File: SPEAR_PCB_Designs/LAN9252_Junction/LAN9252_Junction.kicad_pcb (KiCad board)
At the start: 2 copper layers, 68 parts, among them J1 SM04B-GHS-TB, J3 SM04B-GHS-TB, SW2 SW_MEC_5E, T1 H1102NLT, T2 H1102NLT, U1 LAN9252_ML, U2 24FC512, Y1 25MHz

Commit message: Almost finished board
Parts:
- added C28: 1000 pF, Capacitor_SMD:C_0402_1005Metric, F.Cu at (111.5, 108.8)
- added C29: 1000 pF, Capacitor_SMD:C_0402_1005Metric, F.Cu at (70.3, 38.9)
- added C30: 0.1 uF, Capacitor_SMD:C_0402_1005Metric, F.Cu at (70.1, 60.9)
- added C31: 18pF, Capacitor_SMD:C_0402_1005Metric, F.Cu at (72.0, 69.7)
- added C32: 0.1uF, Capacitor_SMD:C_0402_1005Metric, F.Cu at (107.7, 60.7)
- added C33: 0.1uF, Capacitor_SMD:C_0402_1005Metric, F.Cu at (83.5, 60.8)
- added C34: 18pF, Capacitor_SMD:C_0402_1005Metric, F.Cu at (74.0, 86.5)
- added C35: 0.1uF, Capacitor_SMD:C_0402_1005Metric, F.Cu at (85.2, 60.4)
- added C36: 0.1uF, Capacitor_SMD:C_0402_1005Metric, F.Cu at (87.1, 58.5)
- added C37: 1uF, Capacitor_SMD:C_0402_1005Metric, F.Cu at (100.2, 70.8)
- added C38: 0.1uF, Capacitor_SMD:C_0402_1005Metric, F.Cu at (87.2, 60.4)
- added C39: 0.1uF, Capacitor_SMD:C_0402_1005Metric, F.Cu at (83.9, 64.4)
- added C40: 470 pF, Capacitor_SMD:C_0402_1005Metric, F.Cu at (82.7, 64.5)
- added C41: 0.1uF, Capacitor_SMD:C_0402_1005Metric, F.Cu at (85.9, 67.6)
- added C42: 0.1uF, Capacitor_SMD:C_0402_1005Metric, F.Cu at (99.9, 67.3)
- added C43: 0.1uF, Capacitor_SMD:C_0402_1005Metric, F.Cu at (100.6, 68.9)
- added C44: 0.1uF, Capacitor_SMD:C_0402_1005Metric, F.Cu at (99.7, 79.0)
- added C45: 0.1uF, Capacitor_SMD:C_0402_1005Metric, F.Cu at (85.8, 69.0)
- added C46: 0.1uF, Capacitor_SMD:C_0402_1005Metric, F.Cu at (86.2, 64.2)
- added C47: 0.1uF, Capacitor_SMD:C_0402_1005Metric, F.Cu at (84.6, 77.1)
- added C48: 10p, Capacitor_SMD:C_0402_1005Metric, F.Cu at (108.2, 55.6)
- added C49: 10p, Capacitor_SMD:C_0402_1005Metric, F.Cu at (89.5, 55.6)
- added C50: 10p, Capacitor_SMD:C_0402_1005Metric, F.Cu at (110.5, 55.6)
- added C51: 10p, Capacitor_SMD:C_0402_1005Metric, F.Cu at (87.3, 55.5)
- added C52: 10p, Capacitor_SMD:C_0402_1005Metric, F.Cu at (101.8, 55.6)
- added C53: 10p, Capacitor_SMD:C_0402_1005Metric, F.Cu at (96.0, 55.5)
- added C54: 10p, Capacitor_SMD:C_0402_1005Metric, F.Cu at (104.1, 55.6)
- added C55: 10p, Capacitor_SMD:C_0402_1005Metric, F.Cu at (93.4, 55.5)
- added C56: 22n, Capacitor_SMD:C_0402_1005Metric, F.Cu at (102.2, 60.8)
- added C57: 22n, Capacitor_SMD:C_0402_1005Metric, F.Cu at (80.7, 59.1)
- added C58: 1000 pF, Capacitor_SMD:C_0402_1005Metric, F.Cu at (85.0, 38.8)
- added C59: 1000 pF, Capacitor_SMD:C_0402_1005Metric, F.Cu at (99.7, 38.8)
- added C60: 0.1 uF, Capacitor_SMD:C_0402_1005Metric, F.Cu at (99.4, 68.9)
- added C61: 10uF, Capacitor_SMD:C_0805_2012Metric, F.Cu at (121.6, 91.2)
- added C62: 10uF, Capacitor_SMD:C_0805_2012Metric, F.Cu at (121.6, 94.2)
- added C63: 150nF, SPEAR_MOTORCONTRLLER:CAP_CC1206_YAG, F.Cu at (128.8, 81.6)
- added C64: 22uF, SPEAR_MOTORCONTRLLER:CAP_C3225X7R1C226M250AC, F.Cu at (128.8, 73.8)
- added C65: 22uF, SPEAR_MOTORCONTRLLER:CAP_C3225X7R1C226M250AC, F.Cu at (128.8, 77.8)
- added C66: 0.1uF, Capacitor_SMD:C_0201_0603Metric, F.Cu at (128.2, 122.7)
- added C67: 0.1uF, Capacitor_SMD:C_0201_0603Metric, F.Cu at (138.3, 112.3)
- added D4: LED, LED_SMD:LED_0603_1608Metric, F.Cu at (97.3, 39.0)
- added D5: LED, LED_SMD:LED_0603_1608Metric, F.Cu at (111.9, 39.0)
- added D6: LED, LED_SMD:LED_0603_1608Metric, F.Cu at (113.1, 65.2)
- added F1: 10A, SPEAR_MOTORCONTRLLER:3557-15_KEY, F.Cu at (132.6, 45.1)
- added F2: 15A, SPEAR_MOTORCONTRLLER:3557-15_KEY, F.Cu at (132.6, 53.5)
- added F3: 2A, SPEAR_MOTORCONTRLLER:FUSE_36912000440, F.Cu at (155.1, 45.4)
- added FB5: BLM18EG221SN1D, SPEAR_FOOTPRINTS:Ferrite_bead, F.Cu at (105.3, 61.6)
- added FB6: FerriteBead, SPEAR_FOOTPRINTS:Ferrite_bead, F.Cu at (81.3, 61.1)
- added FB7: BLM18EG221SN1D, SPEAR_FOOTPRINTS:Ferrite_bead, F.Cu at (84.2, 58.2)
- added FB8: BLM18EG221SN1D, SPEAR_FOOTPRINTS:Ferrite_bead, F.Cu at (82.6, 66.2)
- added J2: SM04B-GHS-TB, Connector_JST:JST_GH_SM04B-GHS-TB_1x04-1MP_P1.25mm_Horizontal, F.Cu at (77.0, 39.4)
- added J4: SM04B-GHS-TB, Connector_JST:JST_GH_SM04B-GHS-TB_1x04-1MP_P1.25mm_Horizontal, F.Cu at (106.2, 39.4)
- added J5: Conn_01x02_Pin, SPEAR_MOTORCONTRLLER:AMASS_XT30PW-M_1x02_P2.50mm_Horizontal_1, F.Cu at (138.0, 39.8)
- added J6: Conn_01x02_Pin, SPEAR_MOTORCONTRLLER:AMASS_XT30PW-M_1x02_P2.50mm_Horizontal_1, F.Cu at (153.4, 39.8)
- added R22: 1k, Resistor_SMD:R_0402_1005Metric, F.Cu at (83.2, 41.2)
- added R23: 4.7kR, Resistor_SMD:R_0402_1005Metric, F.Cu at (70.0, 69.7)
- added R24: 10kR, Resistor_SMD:R_0402_1005Metric, F.Cu at (97.8, 96.2)
- added R30: 0R, Resistor_SMD:R_0402_1005Metric, F.Cu at (75.2, 69.7)
- added R31: 12.1k, Resistor_SMD:R_0402_1005Metric, F.Cu at (91.9, 59.1)
- added R32: 141 R, Resistor_SMD:R_0402_1005Metric, F.Cu at (81.6, 68.2)
- added R33: 141 R, Resistor_SMD:R_0402_1005Metric, F.Cu at (167.0, 64.5)
- added R34: 49.9R 1%, Resistor_SMD:R_0402_1005Metric, F.Cu at (108.2, 56.8)
- added R35: 49.9R 1%, Resistor_SMD:R_0402_1005Metric, F.Cu at (89.5, 56.7)
- added R36: 49.9R 1%, Resistor_SMD:R_0402_1005Metric, F.Cu at (110.6, 56.8)
- added R37: 49.9R 1%, Resistor_SMD:R_0402_1005Metric, F.Cu at (87.2, 56.6)
- added R38: 49.9R 1%, Resistor_SMD:R_0402_1005Metric, F.Cu at (101.8, 56.8)
- added R39: 49.9R 1%, Resistor_SMD:R_0402_1005Metric, F.Cu at (96.0, 56.7)
- added R40: 49.9R 1%, Resistor_SMD:R_0402_1005Metric, F.Cu at (104.1, 56.8)
- added R41: 49.9R 1%, Resistor_SMD:R_0402_1005Metric, F.Cu at (93.4, 56.7)
- added R42: 0R, Resistor_SMD:R_0402_1005Metric, F.Cu at (105.6, 60.2)
- added R43: 0R, Resistor_SMD:R_0402_1005Metric, F.Cu at (81.9, 59.1)
- added R44: 1k, Resistor_SMD:R_0402_1005Metric, F.Cu at (97.8, 41.2)
- added R45: 75R 1%, Resistor_SMD:R_0402_1005Metric, F.Cu at (85.0, 40.9)
- added R46: 75R 1%, Resistor_SMD:R_0402_1005Metric, F.Cu at (86.2, 40.9)
- added R47: 75R 1%, Resistor_SMD:R_0402_1005Metric, F.Cu at (99.7, 40.9)
- added R48: 75R 1%, Resistor_SMD:R_0402_1005Metric, F.Cu at (100.8, 40.9)
- added R49: 1k, Resistor_SMD:R_0402_1005Metric, F.Cu at (112.4, 41.2)
- added R50: 4.7kR, Resistor_SMD:R_0402_1005Metric, F.Cu at (110.3, 62.1)
- added R51: 10kR, Resistor_SMD:R_0402_1005Metric, F.Cu at (113.9, 62.5)
- added R52: 10kR, Resistor_SMD:R_0402_1005Metric, F.Cu at (112.4, 42.9)
- added R53: 10kR, Resistor_SMD:R_0402_1005Metric, F.Cu at (97.7, 42.9)
- added R54: 270R, Resistor_SMD:R_0402_1005Metric, F.Cu at (112.9, 62.5)
- added R55: 2kR, Resistor_SMD:R_0402_1005Metric, F.Cu at (105.1, 69.8)
- added R56: 2kR, Resistor_SMD:R_0402_1005Metric, F.Cu at (105.1, 68.6)
- added R57: 10k, Resistor_SMD:R_0402_1005Metric, F.Cu at (124.7, 122.7)
- added R58: 10k, Resistor_SMD:R_0402_1005Metric, F.Cu at (134.9, 112.3)
- added SW1: SW_MEC_5E, Button_Switch_THT:SW_PUSH_6mm, F.Cu at (121.3, 125.0)
- added T3: H1102NLT, SPEAR_FOOTPRINTS:XFMR_H1102NLT, F.Cu at (91.6, 49.0)
- added T4: H1102NLT, SPEAR_FOOTPRINTS:XFMR_H1102NLT, F.Cu at (106.2, 49.0)
- added U3: LAN9252_ML, SPEAR_FOOTPRINTS:LAN9252_QFN UPDATED, F.Cu at (92.1, 66.3)
- added U4: 24FC512, Package_SO:SOIC-8_3.9x4.9mm_P1.27mm, F.Cu at (108.8, 66.4)
- added U5: AP63203WU, SPEAR_MOTORCONTRLLER:AP63203WU-7_DIO-L, F.Cu at (124.7, 62.8)
- added Y2: 25MHz, SPEAR_FOOTPRINTS:Y_Wurth_WE-XTAL_Quartz-HC49-4HSMX, F.Cu at (73.6, 78.2)
- C1: value 1uF -> 18pF; footprint Capacitor_SMD:C_0201_0603Metric -> Capacitor_SMD:C_0402_1005Metric
- C10: value 0.1uF -> 470 pF; footprint Capacitor_SMD:C_0201_0603Metric -> Capacitor_SMD:C_0402_1005Metric
- C11, C12, C13, C14, C15, C16, C17, C2, C5, C8, C9: footprint Capacitor_SMD:C_0201_0603Metric -> Capacitor_SMD:C_0402_1005Metric
- C18, C19, C20, C21, C22: value 0.1uF -> 10p; footprint Capacitor_SMD:C_0201_0603Metric -> Capacitor_SMD:C_0402_1005Metric
- C23, C24: value C -> 10p; footprint Capacitor_SMD:C_0201_0603Metric -> Capacitor_SMD:C_0402_1005Metric
- C25: value 1000 uF -> 10p; footprint Capacitor_SMD:C_0201_0603Metric -> Capacitor_SMD:C_0402_1005Metric
- C26: value 1000 uF -> 22n; footprint Capacitor_SMD:C_0201_0603Metric -> Capacitor_SMD:C_0402_1005Metric
- C27: value 0.1 uF -> 22n; footprint Capacitor_SMD:C_0201_0603Metric -> Capacitor_SMD:C_0402_1005Metric
- C3: value 1uF -> 0.1uF; footprint Capacitor_SMD:C_0201_0603Metric -> Capacitor_SMD:C_0402_1005Metric
- C4: value 0.1uF -> 18pF; footprint Capacitor_SMD:C_0201_0603Metric -> Capacitor_SMD:C_0402_1005Metric
- C6: value 18pF -> 0.1uF; footprint Capacitor_SMD:C_0201_0603Metric -> Capacitor_SMD:C_0402_1005Metric
- C7: value 18pF -> 1uF; footprint Capacitor_SMD:C_0201_0603Metric -> Capacitor_SMD:C_0402_1005Metric
- D1, D2, D3: footprint LED_SMD:LED_0201_0603Metric -> LED_SMD:LED_0603_1608Metric
- FB1, FB2, FB3, FB4: footprint Footprints SPEAR:Ferrite_bead -> SPEAR_FOOTPRINTS:Ferrite_bead
- R1: value 12.1k -> 4K7; footprint Resistor_SMD:R_0603_1608Metric -> Resistor_SMD:R_0402_1005Metric
- R10, R11, R12, R7, R8, R9: value 49.9 R -> 49.9R 1%; footprint Resistor_SMD:R_0603_1608Metric -> Resistor_SMD:R_0402_1005Metric
- R13, R14: value 2kR -> 49.9R 1%; footprint Resistor_SMD:R_0603_1608Metric -> Resistor_SMD:R_0402_1005Metric
- R15: value 4.7kR -> 0R; footprint Resistor_SMD:R_0603_1608Metric -> Resistor_SMD:R_0402_1005Metric
- R16: value 270R -> 0R; footprint Resistor_SMD:R_0603_1608Metric -> Resistor_SMD:R_0402_1005Metric
- R17: value 10kR -> 1k; footprint Resistor_SMD:R_0603_1608Metric -> Resistor_SMD:R_0402_1005Metric
- R18, R19: value 10kR -> 75R 1%; footprint Resistor_SMD:R_0603_1608Metric -> Resistor_SMD:R_0402_1005Metric
- R2: value 10k -> 4K7; footprint Resistor_SMD:R_0603_1608Metric -> Resistor_SMD:R_0402_1005Metric
- R20, R21: value 1k -> 75R 1%; footprint Resistor_SMD:R_0603_1608Metric -> Resistor_SMD:R_0402_1005Metric
- R25: value 0R -> 10kR; footprint Resistor_SMD:R_0603_1608Metric -> Resistor_SMD:R_0402_1005Metric
- R26: value 75 -> 10kR; footprint Resistor_SMD:R_0603_1608Metric -> Resistor_SMD:R_0402_1005Metric
- R27: value 75 -> 270R; footprint Resistor_SMD:R_0603_1608Metric -> Resistor_SMD:R_0402_1005Metric
- R28, R29: value 75 -> 2kR; footprint Resistor_SMD:R_0603_1608Metric -> Resistor_SMD:R_0402_1005Metric
- R3: value 49.9 R -> 0R; footprint Resistor_SMD:R_0603_1608Metric -> Resistor_SMD:R_0402_1005Metric
- R4: value 49.9 R -> 12.1k; footprint Resistor_SMD:R_0603_1608Metric -> Resistor_SMD:R_0402_1005Metric
- R5, R6: value 49.9 R -> 141 R; footprint Resistor_SMD:R_0603_1608Metric -> Resistor_SMD:R_0402_1005Metric
- T1, T2: footprint Transformer_SMD:Transformer_Pulse_H1100NL -> SPEAR_FOOTPRINTS:XFMR_H1102NLT
- U1: footprint Footprints SPEAR:QFP50P1200X1200X120-65N -> SPEAR_FOOTPRINTS:LAN9252_QFN UPDATED
- Y1: footprint Crystal:Crystal_HC50_Vertical -> SPEAR_FOOTPRINTS:Y_Wurth_WE-XTAL_Quartz-HC49-4HSMX
- moved D2 65.7 mm to (82.7, 39.0), turned to -90 degrees
- moved T2 65.1 mm to (76.9, 49.0), turned to 90 degrees
- moved C26 61.5 mm to (70.3, 57.7), turned to 180 degrees
- moved R21 57.9 mm to (71.5, 41.0), turned to 90 degrees
- moved SW2 57.3 mm to (131.4, 115.2)
- moved R20 57.1 mm to (70.3, 41.0), turned to 90 degrees
- moved C24 56.7 mm to (75.1, 55.2)
- moved J3 54.7 mm to (91.5, 39.5), turned to 180 degrees
- moved C22 52.0 mm to (72.5, 55.2), turned to 180 degrees
- moved FB1 51.1 mm to (75.0, 60.4), turned to 90 degrees
- moved R29 50.4 mm to (73.5, 60.4), turned to -90 degrees
- moved R28 49.9 mm to (72.2, 60.4), turned to -90 degrees
- moved U2 48.8 mm to (71.6, 65.2), turned to 90 degrees
- moved R15 47.6 mm to (70.3, 58.9), turned to 180 degrees
- moved C18 44.9 mm to (78.7, 55.1), turned to 180 degrees
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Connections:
- net /D0/SIO0 renamed /LAN9252 System 1/D0/SIO0
- net /D1/SIO1 renamed /LAN9252 System 1/D1/SIO1
- net /D2/SIO2 renamed /LAN9252 System 1/D2/SIO2
- net /D3/SIO3 renamed /LAN9252 System 1/D3/SIO3
- net /D5/OUTVALID/~{SCS} renamed /LAN9252 System 1/D5/OUTVALID/~{SCS}
- net /D7/GPI1/GPO1 renamed /LAN9252 System 1/MII_MDC
- net /D9/LATCH_IN/SCK renamed /LAN9252 System 1/D9/LATCH_IN/SCK
- net /IRQ renamed /LAN9252 System 1/IRQ
- net /SYNC0/LATCH0 renamed /LAN9252 System 1/SYNC0/LATCH0
- net /SYNC1/LATCH1 renamed /LAN9252 System 1/SYNC1/LATCH1
- C1 pad 1: /VDD33TXRX1 -> GND
- C10 pad 1: /VDD12TX1 -> /LAN9252 System 1/VDDCR
- C10 pad 2: GNDREF -> GND
- C11 pad 1: /VDD12TX1 -> +3.3V
- C11 pad 2: GNDREF -> GND
- C12 pad 1: +3.3V -> /LAN9252 System 1/VDDCR
- C12 pad 2: GNDREF -> GND
- C13 pad 2: GNDREF -> GND
- C14 pad 2: GNDREF -> GND
- C15 pad 2: GNDREF -> GND
- C16 pad 2: GNDREF -> GND
- C17 pad 2: GNDREF -> GND
- C18 pad 1: /VDDCR -> /LAN9252 System 1/TXA_P
- C18 pad 2: GNDREF -> GND
- C19 pad 1: /VDDCR -> /LAN9252 System 1/TXB_P
- C19 pad 2: GNDREF -> GND
- C2 pad 1: /VDD33TXRX1 -> /LAN9252 System 1/VDD33TXRX1
- C2 pad 2: Net-(C1-Pad2) -> GND
- C20 pad 1: /VDDCR -> /LAN9252 System 1/TXA_N
- C20 pad 2: GNDREF -> GND
- C21 pad 1: /VDDCR -> /LAN9252 System 1/TXB_N
- C21 pad 2: GNDREF -> GND
- C22 pad 1: /TP3 -> /LAN9252 System 1/RXA_P
- C22 pad 2: GNDREF -> GND
- C23 pad 1: Net-(C23-Pad1) -> /LAN9252 System 1/RXB_P
- C23 pad 2: GNDREF -> GND
- C24 pad 1: Net-(C24-Pad1) -> /LAN9252 System 1/RXA_N
- C24 pad 2: GNDREF -> GND
- C25 pad 1: Net-(C25-Pad1) -> /LAN9252 System 1/RXB_N
- C25 pad 2: GNDREF -> GND
- C26 pad 2: GNDREF -> GND
- C27 pad 1: +3.3V -> Net-(C27-Pad1)
- C27 pad 2: GNDREF -> GND
- C3 pad 1: /VDD33TXRX2 -> /LAN9252 System 1/VDD33TXRX2
- C3 pad 2: Net-(C3-Pad2) -> GND
- C4 pad 1: /VDD33TXRX2 -> GND
- C4 pad 2: Net-(C3-Pad2) -> Net-(U1-OSCO)
- C5 pad 1: +3.3V -> Net-(U1-VDD33BIAS)
- C6 pad 1: GNDREF -> /LAN9252 System 1/VDD12TX1
- C6 pad 2: Net-(C6-Pad2) -> GND
- C7 pad 1: GNDREF -> /LAN9252 System 1/VDDCR
- C7 pad 2: Net-(U1-OSCO) -> GND
- C8 pad 1: /VDD12TX1 -> /LAN9252 System 1/VDD12TX1
- C8 pad 2: GNDREF -> GND
- C9 pad 1: /VDD12TX1 -> /LAN9252 System 1/VDDCR
- C9 pad 2: GNDREF -> GND
- D1 pad 1: Net-(D1-K) -> GND
- D1 pad 2: +3.3V -> Net-(D1-A)
- D2 pad 1: Net-(D2-K) -> GND
- D2 pad 2: GND -> Net-(D2-A)
- D3 pad 2: GND -> +3.3V
- FB1 pad 2: /VDD33TXRX1 -> /LAN9252 System 1/VDD33TXRX1
- FB2 pad 2: /VDD33TXRX2 -> /LAN9252 System 1/VDD33TXRX2
- FB4 pad 1: /VDD12TX1 -> /LAN9252 System 1/VDD12TX1
- FB4 pad 2: /VDDCR -> /LAN9252 System 1/VDDCR
- J1 pad 1: Net-(J1-Pin_1) -> /LAN9252 System 1/LAN9252 Ports/TXB+
- J1 pad 2: Net-(J1-Pin_2) -> /LAN9252 System 1/LAN9252 Ports/TXB-
- J1 pad 3: Net-(J1-Pin_3) -> /LAN9252 System 1/LAN9252 Ports/RXB+
- J1 pad 4: Net-(J1-Pin_4) -> /LAN9252 System 1/LAN9252 Ports/RXB-
- J3 pad 1: Net-(J3-Pin_1) -> /LAN9252 System 2/LAN9252 Ports/TXB+
- J3 pad 2: Net-(J3-Pin_2) -> /LAN9252 System 2/LAN9252 Ports/TXB-
- J3 pad 3: Net-(J3-Pin_3) -> /LAN9252 System 2/LAN9252 Ports/RXB+
- J3 pad 4: Net-(J3-Pin_4) -> /LAN9252 System 2/LAN9252 Ports/RXB-
- R1 pad 1: GNDREF -> /LAN9252 System 1/MII_MDIO
- R1 pad 2: Net-(U1-RBIAS) -> +3.3V
- R10 pad 1: /VDD33TXRX2 -> /LAN9252 System 1/VDD33TXRX2
- R10 pad 2: /RXB_P -> /LAN9252 System 1/TXB_N
- R11 pad 1: /VDD33TXRX2 -> /LAN9252 System 1/VDD33TXRX1
- R11 pad 2: /RXB_N -> /LAN9252 System 1/RXA_P
- R12 pad 1: /VDD33TXRX2 -> /LAN9252 System 1/VDD33TXRX2
- R12 pad 2: Net-(C24-Pad1) -> /LAN9252 System 1/RXB_P
- R13 pad 1: +3.3V -> /LAN9252 System 1/VDD33TXRX1
- R13 pad 2: /I2C_SCL -> /LAN9252 System 1/RXA_N
- R14 pad 1: +3.3V -> /LAN9252 System 1/VDD33TXRX2
- R14 pad 2: /I2C_SDL -> /LAN9252 System 1/RXB_N
- R15 pad 1: GNDREF -> /LAN9252 System 1/VDD33TXRX1
- R15 pad 2: Net-(U2-A0) -> Net-(C26-Pad1)
- R16 pad 1: /GPIO2 -> /LAN9252 System 1/VDD33TXRX2
- R16 pad 2: Net-(D1-K) -> Net-(C27-Pad1)
- R17 pad 1: /GPIO2 -> /LAN9252 System 1/GPIO1
- R17 pad 2: +3.3V -> Net-(D1-A)
- R18 pad 1: GNDREF -> Net-(R18-Pad1)
- R18 pad 2: /GPIO0 -> Net-(C28-Pad1)
- R19 pad 1: GNDREF -> Net-(R19-Pad1)
- R19 pad 2: /GPIO1 -> Net-(C28-Pad1)
- R2 pad 1: +3.3V -> /LAN9252 System 2/MII_MDIO
- R2 pad 2: /TP3 -> +3.3V
- R20 pad 1: /GPIO1 -> Net-(R20-Pad1)
- R20 pad 2: Net-(D2-K) -> Net-(C29-Pad1)
- R21 pad 1: /GPIO0 -> Net-(R21-Pad1)
- R21 pad 2: Net-(D3-K) -> Net-(C29-Pad1)
- R25 pad 1: Net-(C6-Pad2) -> GND
- R25 pad 2: Net-(U1-OSCI) -> /LAN9252 System 1/GPIO0
- R26 pad 1: Net-(R26-Pad1) -> +3.3V
- R26 pad 2: Net-(C26-Pad1) -> /LAN9252 System 1/GPIO1
- R27 pad 1: Net-(R27-Pad1) -> /LAN9252 System 1/GPIO2
- R27 pad 2: Net-(C26-Pad1) -> Net-(D3-K)
- R28 pad 1: Net-(R28-Pad1) -> +3.3V
- R28 pad 2: Net-(C25-Pad1) -> /LAN9252 System 1/I2C_SCL
- R29 pad 1: Net-(R29-Pad1) -> +3.3V
- R29 pad 2: Net-(C25-Pad1) -> /LAN9252 System 1/I2C_SDL
- R3 pad 1: /VDD33TXRX1 -> Net-(C1-Pad2)
- R3 pad 2: /TXA_P -> Net-(U1-OSCI)
- R4 pad 1: /VDD33TXRX1 -> GND
- R4 pad 2: /TXA_N -> Net-(U1-RBIAS)
- R5 pad 1: /VDD33TXRX1 -> /LAN9252 System 1/MII_TXD2
- R5 pad 2: /RXA_P -> GND
- R6 pad 1: /VDD33TXRX1 -> /LAN9252 System 1/MII_TXD3
- R6 pad 2: /RXA_N -> GND
- R7 pad 1: /VDD33TXRX1 -> /LAN9252 System 1/VDD33TXRX1
- R7 pad 2: Net-(C23-Pad1) -> /LAN9252 System 1/TXA_P
- R8 pad 1: /VDD33TXRX2 -> /LAN9252 System 1/VDD33TXRX2
- R8 pad 2: /TXB_P -> /LAN9252 System 1/TXB_P
- R9 pad 1: /VDD33TXRX2 -> /LAN9252 System 1/VDD33TXRX1
- R9 pad 2: /TXB_N -> /LAN9252 System 1/TXA_N
- SW2 pad 1: GNDREF -> GND
- SW2 pad 2: GNDREF -> GND
- SW2 pad 3: /TP3 -> /LAN9252 System 2/TP1
- SW2 pad 4: /TP3 -> /LAN9252 System 2/TP1
- T1 pad 1: /TXB_P -> /LAN9252 System 1/TXB_N
- T1 pad 10: Net-(R27-Pad1) -> Net-(R19-Pad1)
- T1 pad 11: Net-(J3-Pin_3) -> /LAN9252 System 1/LAN9252 Ports/TXB-
- T1 pad 14: Net-(J3-Pin_2) -> /LAN9252 System 1/LAN9252 Ports/RXB+
- T1 pad 15: Net-(R26-Pad1) -> Net-(R18-Pad1)
- T1 pad 16: Net-(J3-Pin_1) -> /LAN9252 System 1/LAN9252 Ports/RXB-
- T1 pad 2: Net-(C24-Pad1) -> Net-(C27-Pad1)
- T1 pad 3: /TXB_N -> /LAN9252 System 1/TXB_P
- T1 pad 6: /RXB_P -> /LAN9252 System 1/RXB_N
- T1 pad 7: Net-(C24-Pad1) -> Net-(C27-Pad1)
- T1 pad 8: /RXB_N -> /LAN9252 System 1/RXB_P
- T1 pad 9: Net-(J3-Pin_4) -> /LAN9252 System 1/LAN9252 Ports/TXB+
- T2 pad 1: /TXA_P -> /LAN9252 System 1/RXA_P
- T2 pad 10: Net-(R29-Pad1) -> Net-(R21-Pad1)
- T2 pad 11: Net-(J1-Pin_3) -> /LAN9252 System 1/LAN9252 Ports/TXA-
- T2 pad 14: Net-(J1-Pin_2) -> /LAN9252 System 1/LAN9252 Ports/RXA+
- T2 pad 15: Net-(R28-Pad1) -> Net-(R20-Pad1)
- T2 pad 16: Net-(J1-Pin_1) -> /LAN9252 System 1/LAN9252 Ports/RXA-
- T2 pad 2: Net-(C23-Pad1) -> Net-(C26-Pad1)
- T2 pad 3: /TXA_N -> /LAN9252 System 1/RXA_N
- T2 pad 6: /RXA_P -> /LAN9252 System 1/TXA_P
- T2 pad 7: Net-(C23-Pad1) -> Net-(C26-Pad1)
- T2 pad 8: /RXA_N -> /LAN9252 System 1/TXA_N
- T2 pad 9: Net-(J1-Pin_4) -> /LAN9252 System 1/LAN9252 Ports/TXA+
- U1 pad 10: unconnected-(U1-FXSDB/FXLOSB/~{FXSDENB}-Pad10) -> GND
- U1 pad 11: unconnected-(U1-~{RST}-Pad11) -> /LAN9252 System 1/RST#
- U1 pad 15: /D14/GPI8/GPO8/~{TX_SHIFT1} -> /LAN9252 System 1/MII_TXD3
- U1 pad 16: /D13/GPI7/GPO7/~{TX_SHIFT0} -> /LAN9252 System 1/MII_TXD2
- U1 pad 21: /D12/GPI6/GPO6 -> /LAN9252 System 1/MII_TXD1
- U1 pad 22: /D11/GPI5/GPO5 -> /LAN9252 System 1/MII_TXD0
- U1 pad 23: /D10/GPI4/GPO4 -> /LAN9252 System 1/MII_TXEN
- U1 pad 24: /VDDCR -> /LAN9252 System 1/VDDCR
- U1 pad 25: unconnected-(U1-A1/ALELO-Pad25) -> /LAN9252 System 1/MII_CLK25
- U1 pad 26: unconnected-(U1-A3/GPI11/GPO11-Pad26) -> /LAN9252 System 1/MII_RXDV
- U1 pad 27: unconnected-(U1-A4/GPI12/GPO12-Pad27) -> /LAN9252 System 1/MII_RXD0
- U1 pad 28: /CS -> /LAN9252 System 1/MII_RXD1
- U1 pad 29: unconnected-(U1-A2/ALEHI/GPI10/GPO10-Pad29) -> /LAN9252 System 1/MII_LINKPOL
- U1 pad 30: /WR/GPI14/GPO14 -> /LAN9252 System 1/MII_RXD2
- U1 pad 31: /RD/GPI15/GPO15 -> /LAN9252 System 1/MII_RXD3
- U1 pad 33: /A0/D15/GPI9/GPO9 -> GND
- U1 pad 36: /D6/GPI0/GPO0 -> /LAN9252 System 1/MII_RXCLK
- U1 pad 38: /VDDCR -> /LAN9252 System 1/VDDCR
- U1 pad 4: GNDREF -> GND
- U1 pad 40: /D8/GPI2/GPO2 -> /LAN9252 System 1/MII_MDIO
- U1 pad 41: GNDREF -> GND
- U1 pad 42: /I2C_SDL -> /LAN9252 System 1/I2C_SDL
- U1 pad 43: /I2C_SCL -> /LAN9252 System 1/I2C_SCL
- U1 pad 45: /GPIO2 -> /LAN9252 System 1/GPIO2
- U1 pad 46: /GPIO1 -> /LAN9252 System 1/GPIO1
- U1 pad 48: /GPIO0 -> /LAN9252 System 1/GPIO0
- U1 pad 49: /D4/GPI3/GPO3 -> /LAN9252 System 1/MII_LINK
- U1 pad 51: /VDD33TXRX1 -> /LAN9252 System 1/VDD33TXRX1
- U1 pad 52: /TXA_N -> /LAN9252 System 1/TXA_N
- U1 pad 53: /TXA_P -> /LAN9252 System 1/TXA_P
- U1 pad 54: /RXA_N -> /LAN9252 System 1/RXA_N
- U1 pad 55: /RXA_P -> /LAN9252 System 1/RXA_P
- U1 pad 56: /VDD12TX1 -> /LAN9252 System 1/VDD12TX1
- U1 pad 59: /VDD12TX1 -> /LAN9252 System 1/VDD12TX1
- U1 pad 6: /VDDCR -> /LAN9252 System 1/VDDCR
- U1 pad 60: /RXB_P -> /LAN9252 System 1/RXB_P
- U1 pad 61: /RXB_N -> /LAN9252 System 1/RXB_N
- U1 pad 62: /TXB_P -> /LAN9252 System 1/TXB_P
- U1 pad 63: /TXB_N -> /LAN9252 System 1/TXB_N
- U1 pad 64: /VDD33TXRX2 -> /LAN9252 System 1/VDD33TXRX2
- U1 pad 65: GNDREF -> GND
- U1 pad 8: GNDREF -> GND
- U1 pad 9: GNDREF -> GND
- U2 pad 4: GNDREF -> GND
- U2 pad 5: /I2C_SDL -> /LAN9252 System 1/I2C_SDL
- U2 pad 6: /I2C_SCL -> /LAN9252 System 1/I2C_SCL
- Y1 pad 2: Net-(C6-Pad2) -> Net-(C1-Pad2)
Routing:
- net GND: track 0.00 -> 83.2 mm, vias 0 -> 66
- net /LAN9252 System 1/GPIO0: track 0.00 -> 54.8 mm, vias 0 -> 2
- net +3.3V: track 0.00 -> 53.8 mm, vias 0 -> 27
- net /LAN9252 System 1/RXA_P: track 0.00 -> 48.5 mm
- net /LAN9252 System 1/VDD33TXRX1: track 0.00 -> 47.5 mm, vias 0 -> 3
- net /LAN9252 System 1/MII_LINK: track 0.00 -> 47.0 mm, vias 0 -> 2
- net /LAN9252 System 1/RXA_N: track 0.00 -> 46.0 mm
- net /LAN9252 System 1/TXA_P: track 0.00 -> 44.7 mm
- net /LAN9252 System 1/TXA_N: track 0.00 -> 43.8 mm
- net /LAN9252 System 1/GPIO1: track 0.00 -> 36.8 mm, vias 0 -> 3
- net /LAN9252 System 2/GPIO0: track 0.00 -> 36.8 mm, vias 0 -> 2
- net Net-(U3-OSCO): track 0.00 -> 35.9 mm, vias 0 -> 2
- net /LAN9252 System 2/VDDCR: track 0.00 -> 35.3 mm, vias 0 -> 4
- net /LAN9252 System 2/VDD33TXRX1: track 0.00 -> 32.7 mm, vias 0 -> 4
- net /LAN9252 System 1/VDD33TXRX2: track 0.00 -> 31.0 mm, vias 0 -> 4
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- added copper zone on In2.Cu, net +3.3V
- added copper zone on In1.Cu, net GND
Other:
- board outline added: 48 x 74.8 mm
- copper layers 2 -> 4

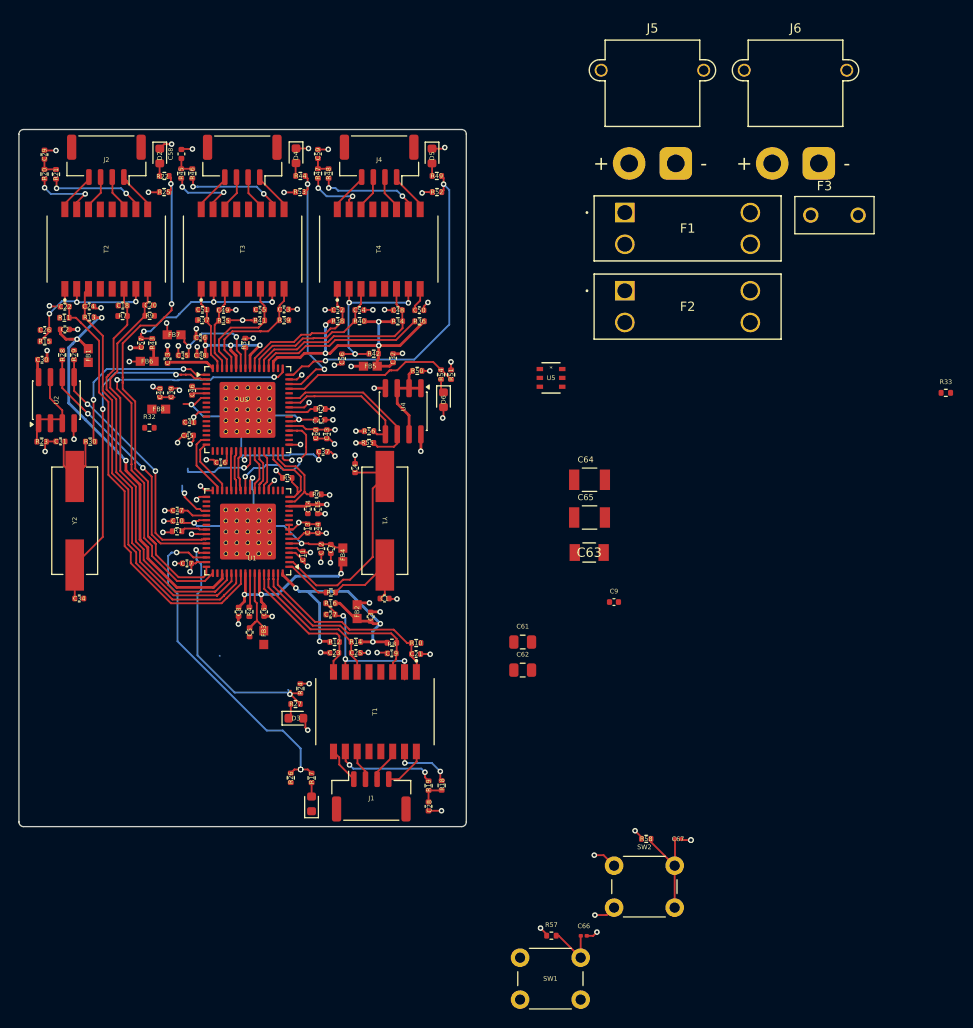
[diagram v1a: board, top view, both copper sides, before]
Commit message: Updated Junction board
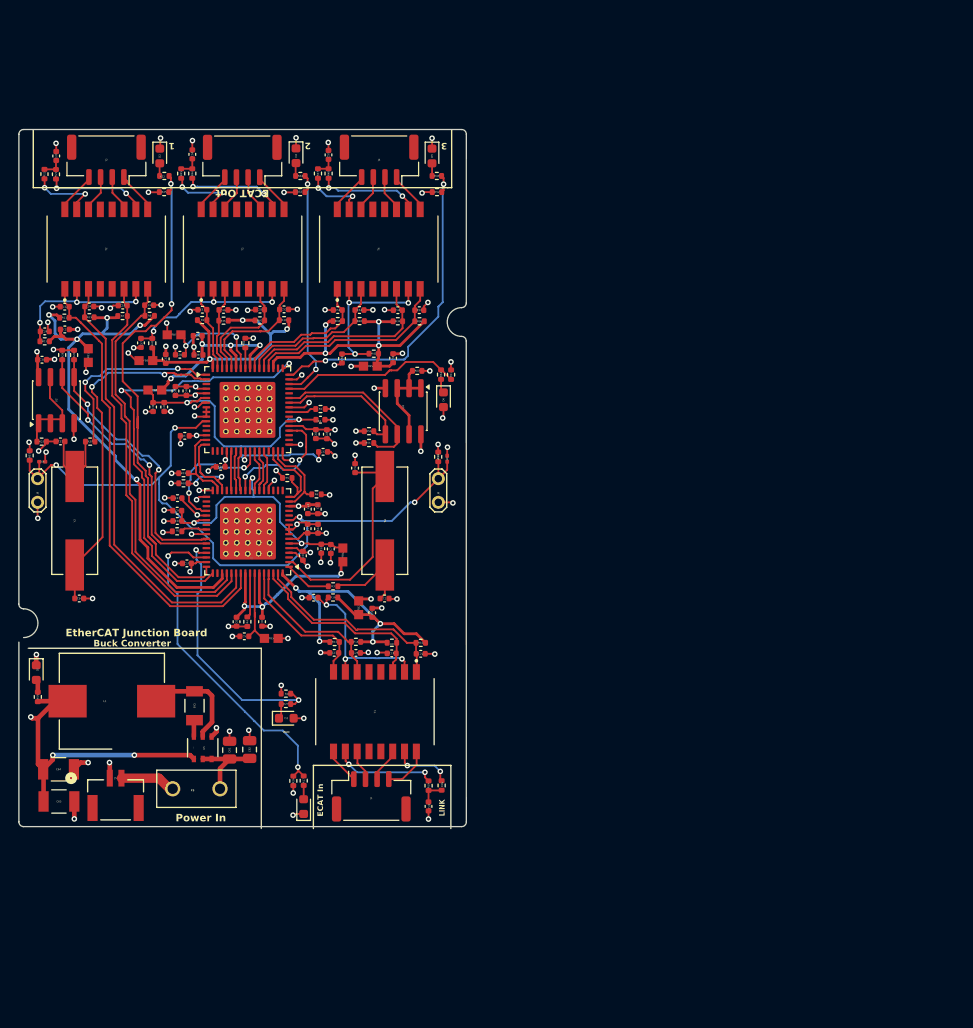
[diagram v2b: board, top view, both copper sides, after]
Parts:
- removed F1: 10A, SPEAR_MOTORCONTRLLER:3557-15_KEY
- removed F2: 15A, SPEAR_MOTORCONTRLLER:3557-15_KEY
- removed J6: Conn_01x02_Pin, SPEAR_MOTORCONTRLLER:AMASS_XT30PW-M_1x02_P2.50mm_Horizontal_1
- removed SW1, SW2: SW_MEC_5E, Button_Switch_THT:SW_PUSH_6mm
- added D7: LED, LED_SMD:LED_0603_1608Metric, F.Cu at (69.4, 94.5)
- added J8: Conn_01x02_Pin, TestPoint:TestPoint_2Pads_Pitch2.54mm_Drill0.8mm, F.Cu at (112.6, 73.7)
- added J9: Conn_01x02_Pin, TestPoint:TestPoint_2Pads_Pitch2.54mm_Drill0.8mm, F.Cu at (69.6, 73.7)
- added L1: 3.9uH, SPEAR_BUCK_CONVERTER:L_Wurth_WE-LHMI-1040_L1, F.Cu at (77.5, 97.5)
- added R59: 1k, Resistor_SMD:R_0402_1005Metric, F.Cu at (69.6, 97.1)
- J5: value Conn_01x02_Pin -> SM02B-GHS-TB; footprint SPEAR_MOTORCONTRLLER:AMASS_XT30PW-M_1x02_P2.50mm_Horizontal_1 -> SPEAR_POWERJUCTION:CONN_SM02B-GHS_JST
- moved F3 92.1 mm to (86.6, 106.9), turned to 180 degrees
- moved J5 91.0 mm to (77.9, 108.1)
- moved R33 82.2 mm to (85.2, 73.1), turned to 180 degrees
- moved C66 77.2 mm to (70.1, 71.8)
- moved R57 76.1 mm to (68.7, 71.2), turned to -90 degrees
- moved C64 64.9 mm to (71.8, 104.8)
- moved C65 64.6 mm to (71.9, 108.3)
- moved U5 54.5 mm to (87.3, 102.5), turned to 90 degrees
- moved C9 47.9 mm to (84.6, 77.1), turned to 180 degrees
- moved C67 47.7 mm to (113.5, 71.5), turned to 90 degrees
- moved R58 46.7 mm to (112.6, 71.3), turned to -90 degrees
- moved C63 45.4 mm to (86.4, 98.0), turned to -90 degrees
- moved C61 33.5 mm to (90.2, 102.8), turned to 90 degrees
- moved C62 30.5 mm to (92.3, 102.7), turned to 90 degrees
- moved R32 6.99 mm to (85.2, 74.2), turned to 180 degrees
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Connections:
- C66 pad 1: /LAN9252 System 1/TP1 -> /LAN9252 System 1/RST
- C67 pad 1: /LAN9252 System 2/TP1 -> /LAN9252 System 1/RST
- F3 pad 2: Net-(J6-Pin_2) -> Net-(F3-Pad2)
- J5 pad 2: Net-(J5-Pin_2) -> Net-(F3-Pad2)
- R57 pad 2: /LAN9252 System 1/TP1 -> /LAN9252 System 1/RST
- R58 pad 2: /LAN9252 System 2/TP1 -> /LAN9252 System 1/RST
- U1 pad 11: /LAN9252 System 1/RST# -> /LAN9252 System 1/RST
- U1 pad 49: /LAN9252 System 1/MII_LINK -> +3.3V
- U3 pad 11: /LAN9252 System 1/RST# -> /LAN9252 System 1/RST
- U3 pad 49: /LAN9252 System 1/MII_LINK -> +3.3V
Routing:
- net +3.3V: track 53.8 -> 145.7 mm, vias 27 -> 41
- net /LAN9252 System 1/RST: track 0.00 -> 77.8 mm, vias 0 -> 4
- net /LAN9252 System 1/MII_LINK: track 47.0 -> 0.00 mm, vias 2 -> 0
- net /LAN9252 System 2/VDD33TXRX2: track 9.59 -> 31.8 mm, vias 1 -> 3
- net GND: track 83.2 -> 104.8 mm, vias 66 -> 84
- net /LAN9252 System 1/VDD33TXRX1: track 47.5 -> 64.0 mm, vias 3 -> 5
- net /Buck Converter/SW: track 0.00 -> 11.6 mm
- net /LAN9252 System 2/TP1: track 11.3 -> 0.00 mm
- net /Buck Converter/BUCK_PWR: track 0.00 -> 9.92 mm
- net /LAN9252 System 2/VDD12TX1: track 13.5 -> 21.5 mm, vias 3 -> 4
- net Net-(F3-Pad2): track 0.00 -> 5.97 mm
- net /LAN9252 System 1/TP1: track 5.96 -> 0.00 mm
- net /LAN9252 System 1/VDD33TXRX2: track 31.0 -> 36.7 mm
- net /LAN9252 System 1/MII_RXD2: track 6.19 -> 11.7 mm, vias 0 -> 2
- net /LAN9252 System 2/VDDCR: track 35.3 -> 40.2 mm
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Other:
- outline, holes or cut-outs redrawn
- board text added: "1"
- board text added: "2"
- board text added: "3"
- board text added: "Buck Converter"
- board text added: "ECAT In"
- board text added: "ECAT Out"
- board text added: "EtherCAT Junction Board"
- board text added: "LINK"
- board text added: "Power In"
- board text added: "RUN"

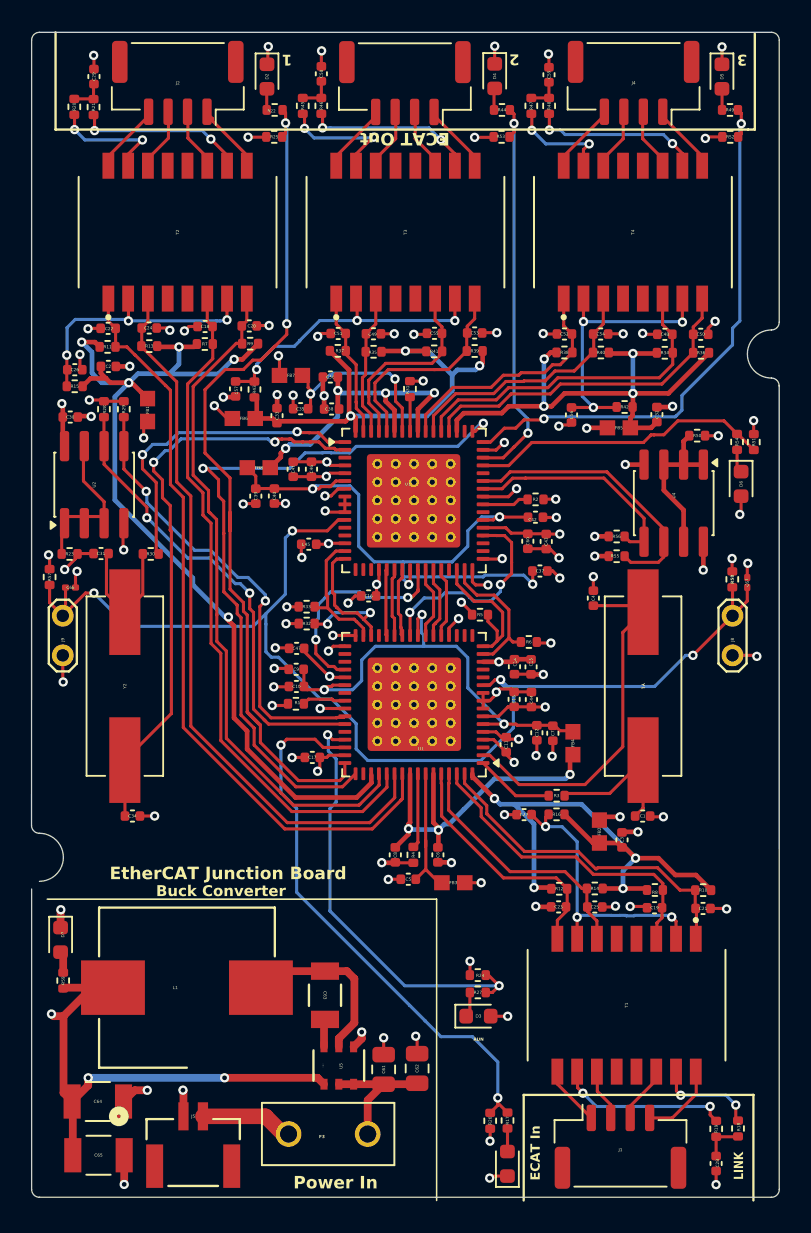
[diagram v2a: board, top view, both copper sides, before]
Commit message: Updated Junction Board
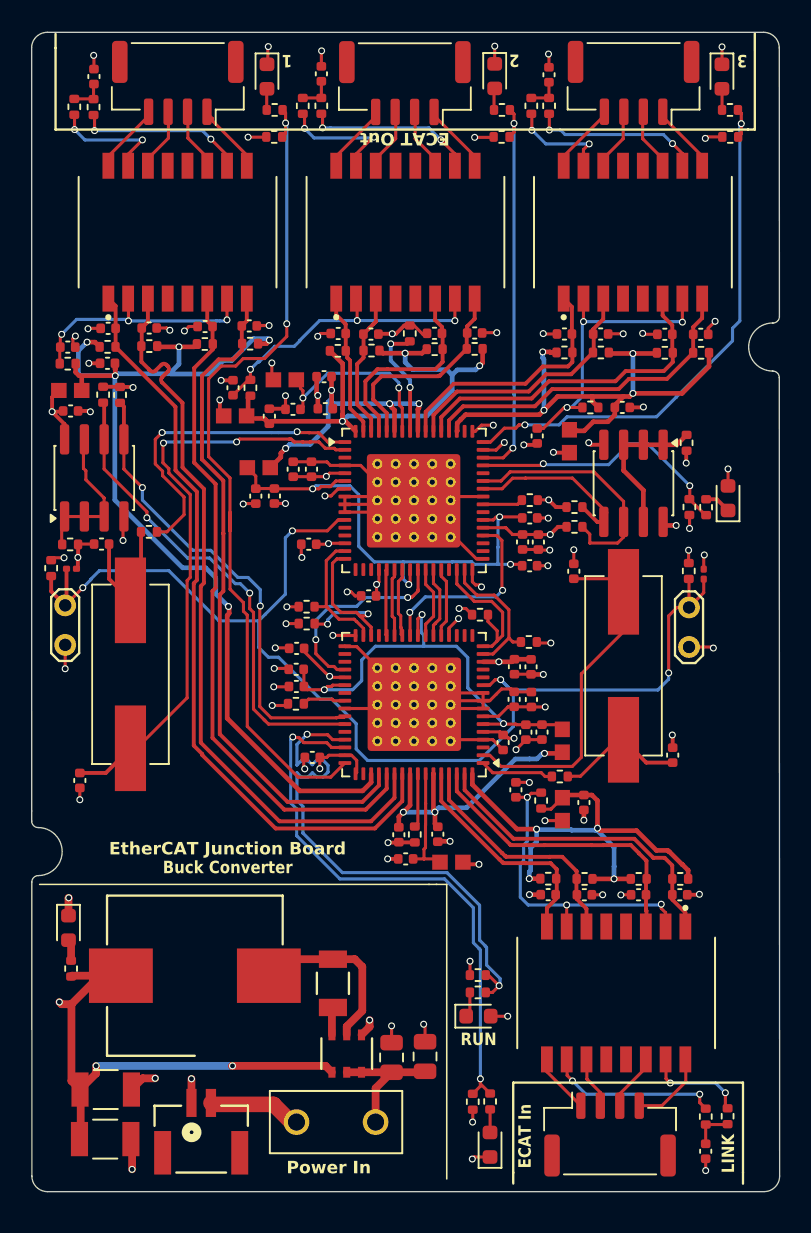
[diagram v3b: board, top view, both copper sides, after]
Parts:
- added G***: LOGO, SPEAR_logos:spear_logo_10.0x10, B.Cu at (104.6, 98.2)
- moved R51 5.88 mm to (109.8, 66.7), turned to -90 degrees
- moved FB1 5.12 mm to (70.1, 59.2), turned to 0 degrees
- moved R54 4.64 mm to (110.9, 66.7), turned to 90 degrees
- moved C1 4.36 mm to (108.7, 82.6), turned to -90 degrees
- moved C34 4.08 mm to (70.7, 84.2), turned to 90 degrees
- moved R31 3.57 mm to (91.8, 55.5)
- moved C3 3.43 mm to (103.0, 85.6), turned to -90 degrees
- moved R55 3.30 mm to (102.4, 67.9)
- moved R56 3.30 mm to (102.4, 66.7)
- moved FB5 3.29 mm to (102.1, 62.4), turned to 90 degrees
- moved U4 2.88 mm to (106.2, 65.2)
- moved C67 2.84 mm to (110.7, 71.0)
- moved J8 2.84 mm to (109.8, 73.1)
- moved R58 2.84 mm to (109.8, 70.8)
- moved FB2 2.78 mm to (101.6, 86.1), turned to 90 degrees
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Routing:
- net +3.3V: track 145.7 -> 97.9 mm, vias 41 -> 37
- net GND: track 104.8 -> 141.6 mm, vias 84 -> 71
- net /LAN9252 System 1/GPIO2: track 28.0 -> 35.5 mm
- net /LAN9252 System 2/VDDCR: track 40.2 -> 33.3 mm
- net Net-(U3-RBIAS): track 2.27 -> 7.42 mm, vias 0 -> 2
- net /LAN9252 System 1/VDD12TX1: track 23.2 -> 19.5 mm
- net /LAN9252 System 2/I2C_SDL: track 14.6 -> 10.9 mm
- net /LAN9252 System 1/VDD33TXRX2: track 36.7 -> 33.7 mm
- net Net-(U1-OSCO): track 24.6 -> 21.8 mm
- net /LAN9252 System 2/I2C_SCL: track 18.0 -> 15.5 mm
- net /LAN9252 System 2/VDD33TXRX1: track 32.7 -> 35.1 mm
- net Net-(C27-Pad1): track 19.0 -> 21.4 mm
- net /LAN9252 System 1/RXA_N: track 46.7 -> 48.7 mm
- net /LAN9252 System 2/VDD12TX1: track 21.5 -> 19.6 mm
- net /LAN9252 System 2/GPIO2: track 19.5 -> 17.6 mm, vias 0 -> 2
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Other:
- board size 48 x 74.8 mm -> 48 x 74.4 mm
- board text added: "Chris Rivington Henry Diep Oliver Schneider"
- board text added: "Space Exploration Alberta Robotics 2026"

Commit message: Updated Gerber files
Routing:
- net /LAN9252 System 1/GPIO2: track 35.5 -> 30.7 mm
